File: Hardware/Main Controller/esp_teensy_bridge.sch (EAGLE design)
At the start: 67 parts, among them IC1 BQ79600PWRQ1, Q5 VISHAY_SIS862DN-T1-GE3VISHAY_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, Q6 VISHAY_SIS862DN-T1-GE3VISHAY_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, Q7 VISHAY_SIS862DN-T1-GE3VISHAY_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, Q8 VISHAY_SIS862DN-T1-GE3VISHAY_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, U1 MCP2562-E/SN, U2 ESP32-DEVKITC-32D, X1 5566-12

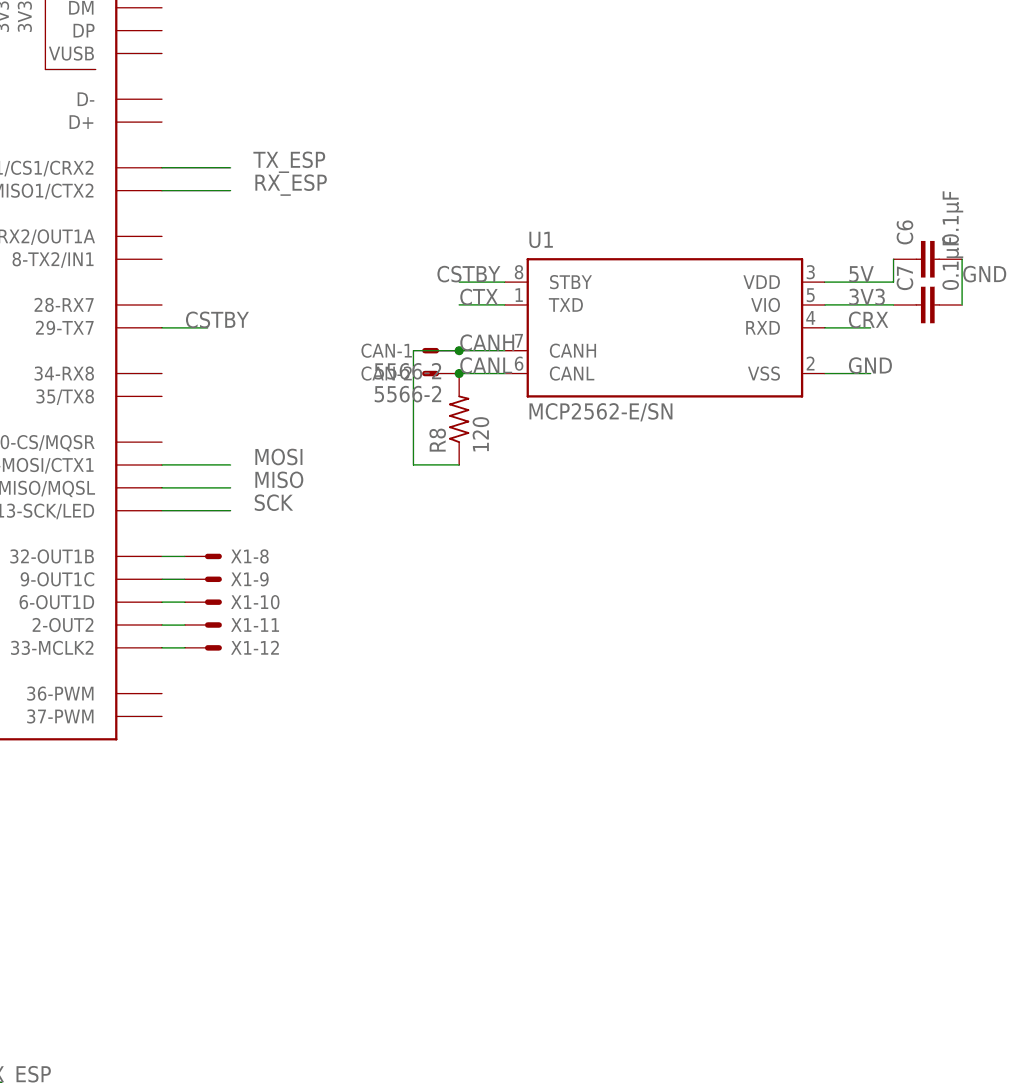
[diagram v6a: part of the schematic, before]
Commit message: tactile switch
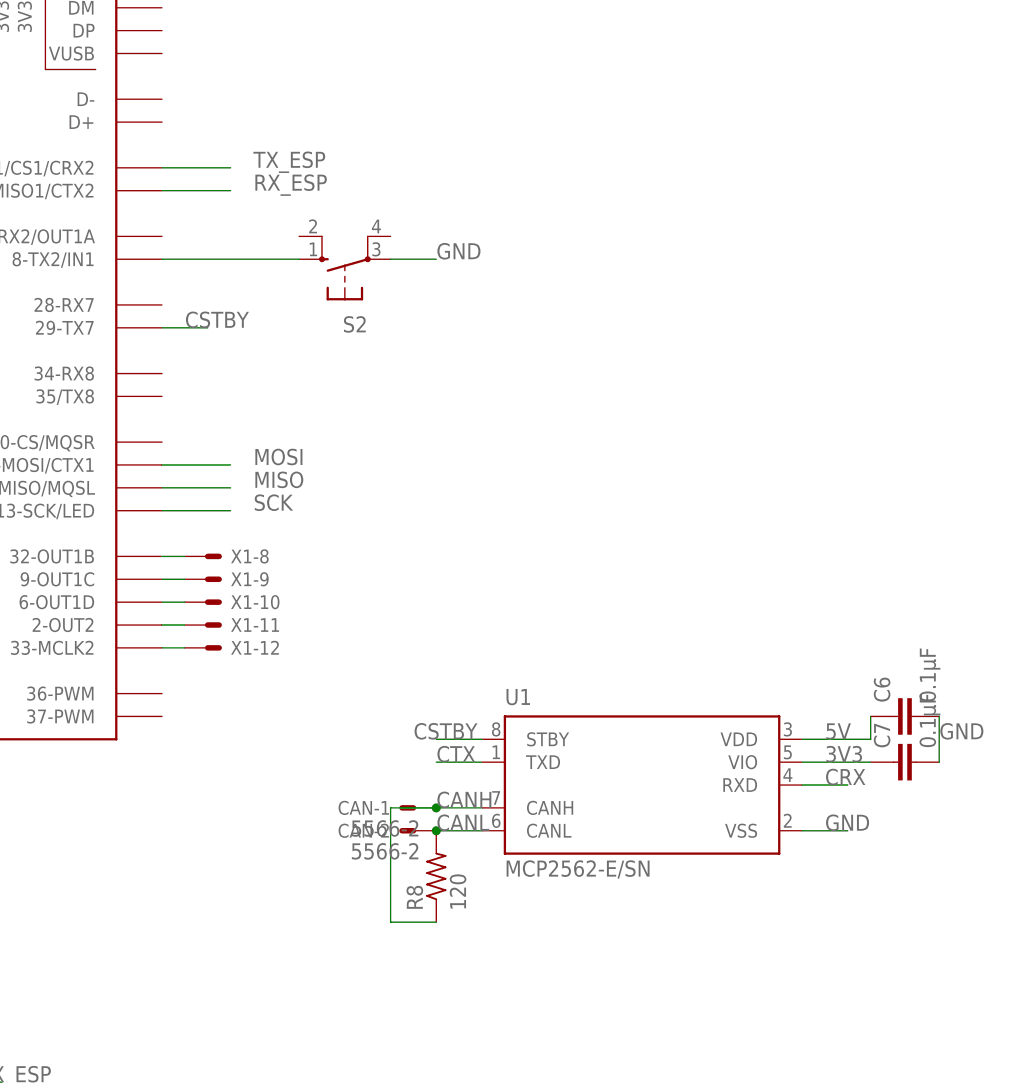
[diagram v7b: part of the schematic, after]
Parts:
- added S2: (no value), switch-omron:10-XX
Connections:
- new net N$7: S2.S, U$3.8-TX2/IN1
- net GND: now also S2.P
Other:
- moved on the sheet: C6, C7, CAN-1, CAN-2, R8, U1
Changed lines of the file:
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@@
 <part name="R8" library="rcl" library_urn="urn:adsk.eagle:library:334" deviceset="R-US_" device="R0603" package3d_urn="urn:adsk.eagle:package:23555/3" value="120"/>
 <part name="U2" library="ESP32-DEVKITC-32D" deviceset="ESP32-DEVKITC-32D" device=""/>
+<part name="S2" library="switch-omron" library_urn="urn:adsk.eagle:library:377" deviceset="10-XX" device="" package3d_urn="urn:adsk.eagle:package:27496/1"/>
 </parts>
 <sheets>
@@
 <attribute name="NAME" x="-126.238" y="-7.62" size="2.54" layer="95" align="top-left"/>
 </instance>
-<instance part="U1" gate="G$1" x="152.4" y="83.82" smashed="yes">
-<attribute name="NAME" x="137.1485" y="92.71671875" size="1.779340625" layer="95"/>
-<attribute name="VALUE" x="137.1361" y="73.6441" size="1.78078125" layer="96"/>
-</instance>
-<instance part="CAN" gate="-1" x="127" y="81.28" smashed="yes" rot="R180">
-<attribute name="NAME" x="124.46" y="82.042" size="1.524" layer="95" rot="R180"/>
-<attribute name="VALUE" x="127.762" y="79.883" size="1.778" layer="96" rot="R180"/>
-</instance>
-<instance part="CAN" gate="-2" x="127" y="78.74" smashed="yes" rot="R180">
-<attribute name="NAME" x="124.46" y="79.502" size="1.524" layer="95" rot="R180"/>
-<attribute name="VALUE" x="127.762" y="77.343" size="1.778" layer="96" rot="R180"/>
-</instance>
-<instance part="C6" gate="G$1" x="180.34" y="91.44" smashed="yes" rot="R90">
-<attribute name="NAME" x="179.959" y="92.964" size="1.778" layer="95" rot="R90"/>
-<attribute name="VALUE" x="185.039" y="92.964" size="1.778" layer="96" rot="R90"/>
-</instance>
-<instance part="C7" gate="G$1" x="180.34" y="86.36" smashed="yes" rot="R90">
-<attribute name="NAME" x="179.959" y="87.884" size="1.778" layer="95" rot="R90"/>
-<attribute name="VALUE" x="185.039" y="87.884" size="1.778" layer="96" rot="R90"/>
-</instance>
-<instance part="R8" gate="G$1" x="129.54" y="73.66" smashed="yes" rot="R90">
-<attribute name="NAME" x="128.0414" y="69.85" size="1.778" layer="95" rot="R90"/>
-<attribute name="VALUE" x="132.842" y="69.85" size="1.778" layer="96" rot="R90"/>
+<instance part="U1" gate="G$1" x="149.86" y="33.02" smashed="yes">
+<attribute name="NAME" x="134.6085" y="41.91671875" size="1.779340625" layer="95"/>
+<attribute name="VALUE" x="134.5961" y="22.8441" size="1.78078125" layer="96"/>
+</instance>
+<instance part="CAN" gate="-1" x="124.46" y="30.48" smashed="yes" rot="R180">
+<attribute name="NAME" x="121.92" y="31.242" size="1.524" layer="95" rot="R180"/>
+<attribute name="VALUE" x="125.222" y="29.083" size="1.778" layer="96" rot="R180"/>
+</instance>
+<instance part="CAN" gate="-2" x="124.46" y="27.94" smashed="yes" rot="R180">
+<attribute name="NAME" x="121.92" y="28.702" size="1.524" layer="95" rot="R180"/>
+<attribute name="VALUE" x="125.222" y="26.543" size="1.778" layer="96" rot="R180"/>
+</instance>
+<instance part="C6" gate="G$1" x="177.8" y="40.64" smashed="yes" rot="R90">
+<attribute name="NAME" x="177.419" y="42.164" size="1.778" layer="95" rot="R90"/>
+<attribute name="VALUE" x="182.499" y="42.164" size="1.778" layer="96" rot="R90"/>
+</instance>
+<instance part="C7" gate="G$1" x="177.8" y="35.56" smashed="yes" rot="R90">
+<attribute name="NAME" x="177.419" y="37.084" size="1.778" layer="95" rot="R90"/>
+<attribute name="VALUE" x="182.499" y="37.084" size="1.778" layer="96" rot="R90"/>
+</instance>
+<instance part="R8" gate="G$1" x="127" y="22.86" smashed="yes" rot="R90">
+<attribute name="NAME" x="125.5014" y="19.05" size="1.778" layer="95" rot="R90"/>
+<attribute name="VALUE" x="130.302" y="19.05" size="1.778" layer="96" rot="R90"/>
 </instance>
 <instance part="U2" gate="G$1" x="53.34" y="-15.24" smashed="yes">
 <attribute name="NAME" x="38.0828" y="10.8243" size="1.78" layer="95"/>
 <attribute name="VALUE" x="38.0837" y="-43.2098" size="1.7799" layer="96"/>
+</instance>
+<instance part="S2" gate="1" x="116.84" y="91.44" smashed="yes" rot="R90">
+<attribute name="NAME" x="119.38" y="85.09" size="1.778" layer="95" rot="R180"/>
+<attribute name="VALUE" x="113.665" y="87.63" size="1.778" layer="96" rot="R180"/>
 </instance>
 </instances>
@@
 <segment>
 <pinref part="U1" gate="G$1" pin="VSS"/>
-<wire x1="170.18" y1="78.74" x2="175.26" y2="78.74" width="0.1524" layer="91"/>
-<label x="172.72" y="78.74" size="1.778" layer="95"/>
+<wire x1="167.64" y1="27.94" x2="172.72" y2="27.94" width="0.1524" layer="91"/>
+<label x="170.18" y="27.94" size="1.778" layer="95"/>
 </segment>
 <segment>
 <pinref part="C6" gate="G$1" pin="2"/>
 <pinref part="C7" gate="G$1" pin="2"/>
-<wire x1="185.42" y1="91.44" x2="185.42" y2="86.36" width="0.1524" layer="91"/>
-<label x="185.42" y="88.9" size="1.778" layer="95"/>
+<wire x1="182.88" y1="40.64" x2="182.88" y2="35.56" width="0.1524" layer="91"/>
+<label x="182.88" y="38.1" size="1.778" layer="95"/>
 </segment>
 <segment>
@@
 <wire x1="33.02" y1="-25.4" x2="25.4" y2="-25.4" width="0.1524" layer="91"/>
 <label x="25.4" y="-25.4" size="1.778" layer="95"/>
+</segment>
+<segment>
+<pinref part="S2" gate="1" pin="P"/>
+<wire x1="121.92" y1="91.44" x2="127" y2="91.44" width="0.1524" layer="91"/>
+<label x="127" y="91.44" size="1.778" layer="95"/>
 </segment>
 </net>
@@
 <segment>
 <pinref part="U1" gate="G$1" pin="VDD"/>
-<wire x1="170.18" y1="88.9" x2="177.8" y2="88.9" width="0.1524" layer="91"/>
-<label x="172.72" y="88.9" size="1.778" layer="95"/>
+<wire x1="167.64" y1="38.1" x2="175.26" y2="38.1" width="0.1524" layer="91"/>
+<label x="170.18" y="38.1" size="1.778" layer="95"/>
 <pinref part="C6" gate="G$1" pin="1"/>
-<wire x1="177.8" y1="88.9" x2="177.8" y2="91.44" width="0.1524" layer="91"/>
+<wire x1="175.26" y1="38.1" x2="175.26" y2="40.64" width="0.1524" layer="91"/>
 </segment>
 <segment>
@@
 <segment>
 <pinref part="U1" gate="G$1" pin="VIO"/>
-<wire x1="170.18" y1="86.36" x2="177.8" y2="86.36" width="0.1524" layer="91"/>
-<label x="172.72" y="86.36" size="1.778" layer="95"/>
+<wire x1="167.64" y1="35.56" x2="175.26" y2="35.56" width="0.1524" layer="91"/>
+<label x="170.18" y="35.56" size="1.778" layer="95"/>
 <pinref part="C7" gate="G$1" pin="1"/>
 </segment>
@@
 <segment>
 <pinref part="U1" gate="G$1" pin="RXD"/>
-<wire x1="170.18" y1="83.82" x2="175.26" y2="83.82" width="0.1524" layer="91"/>
-<label x="172.72" y="83.82" size="1.778" layer="95"/>
+<wire x1="167.64" y1="33.02" x2="172.72" y2="33.02" width="0.1524" layer="91"/>
+<label x="170.18" y="33.02" size="1.778" layer="95"/>
 </segment>
 </net>
@@
 <segment>
 <pinref part="U1" gate="G$1" pin="TXD"/>
-<wire x1="134.62" y1="86.36" x2="129.54" y2="86.36" width="0.1524" layer="91"/>
-<label x="129.54" y="86.36" size="1.778" layer="95"/>
+<wire x1="132.08" y1="35.56" x2="127" y2="35.56" width="0.1524" layer="91"/>
+<label x="127" y="35.56" size="1.778" layer="95"/>
 </segment>
 </net>
@@
 <segment>
 <pinref part="U1" gate="G$1" pin="STBY"/>
-<wire x1="134.62" y1="88.9" x2="129.54" y2="88.9" width="0.1524" layer="91"/>
-<label x="127" y="88.9" size="1.778" layer="95"/>
+<wire x1="132.08" y1="38.1" x2="127" y2="38.1" width="0.1524" layer="91"/>
+<label x="124.46" y="38.1" size="1.778" layer="95"/>
 </segment>
 </net>
@@
 <pinref part="U1" gate="G$1" pin="CANH"/>
 <pinref part="CAN" gate="-1" pin="S"/>
-<wire x1="134.62" y1="81.28" x2="129.54" y2="81.28" width="0.1524" layer="91"/>
-<label x="129.54" y="81.28" size="1.778" layer="95"/>
-<wire x1="129.54" y1="81.28" x2="124.46" y2="81.28" width="0.1524" layer="91"/>
-<wire x1="124.46" y1="81.28" x2="124.46" y2="68.58" width="0.1524" layer="91"/>
-<junction x="129.54" y="81.28"/>
+<wire x1="132.08" y1="30.48" x2="127" y2="30.48" width="0.1524" layer="91"/>
+<label x="127" y="30.48" size="1.778" layer="95"/>
+<wire x1="127" y1="30.48" x2="121.92" y2="30.48" width="0.1524" layer="91"/>
+<wire x1="121.92" y1="30.48" x2="121.92" y2="17.78" width="0.1524" layer="91"/>
+<junction x="127" y="30.48"/>
 <pinref part="R8" gate="G$1" pin="1"/>
-<wire x1="124.46" y1="68.58" x2="129.54" y2="68.58" width="0.1524" layer="91"/>
+<wire x1="121.92" y1="17.78" x2="127" y2="17.78" width="0.1524" layer="91"/>
 </segment>
 </net>
@@
 <pinref part="U1" gate="G$1" pin="CANL"/>
 <pinref part="CAN" gate="-2" pin="S"/>
-<wire x1="134.62" y1="78.74" x2="129.54" y2="78.74" width="0.1524" layer="91"/>
-<label x="129.54" y="78.74" size="1.778" layer="95"/>
+<wire x1="132.08" y1="27.94" x2="127" y2="27.94" width="0.1524" layer="91"/>
+<label x="127" y="27.94" size="1.778" layer="95"/>
 <pinref part="R8" gate="G$1" pin="2"/>
-<junction x="129.54" y="78.74"/>
-</segment>
-</net>
+<junction x="127" y="27.94"/>
+</segment>
+</net>
+<net name="N$7" class="0">
+<segment>
+<pinref part="S2" gate="1" pin="S"/>
+<pinref part="U$3" gate="G$1" pin="8-TX2/IN1"/>
+<wire x1="111.76" y1="91.44" x2="96.52" y2="91.44" width="0.1524" layer="91"/>
+</segment>
+</net>
